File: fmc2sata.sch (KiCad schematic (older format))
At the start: 58 parts, among them J1 ASP-134488-01, J2 1-2199230-6, J3 te-770829-1, Q1 BSS138APW, Q2 BSS138APW, Q3 DMG2305UX-13, Q4 BSS138APW, U1 TPS565208, U2 TPS565208, Y1 AX3DAF1-150.0000

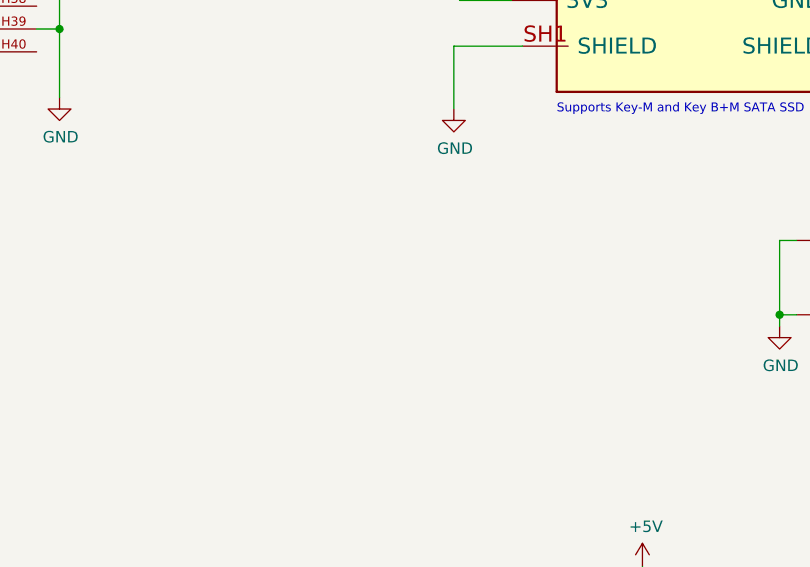
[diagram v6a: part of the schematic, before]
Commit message: Add filtering caps
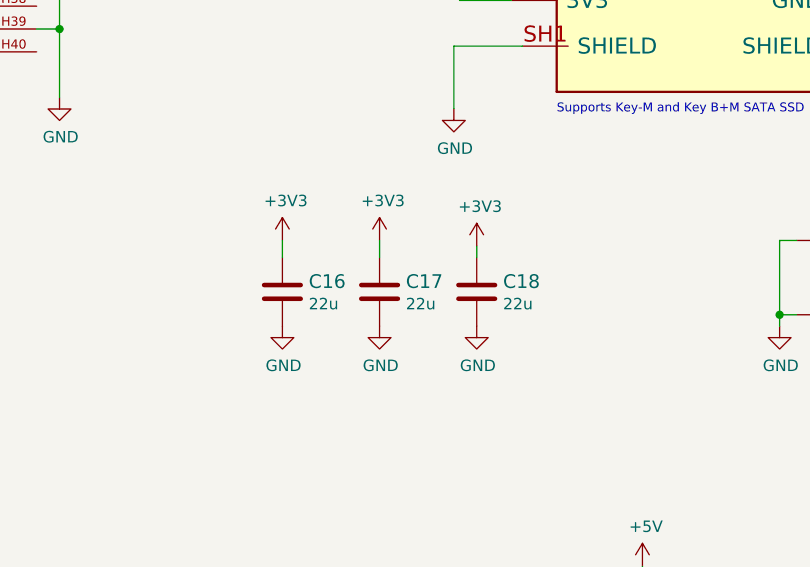
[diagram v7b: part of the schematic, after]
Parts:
- added C16, C17, C18: C_22u_0805_10V, fmc2sata-footprints:0805-cap, symbol fmc2sata:C_22u_0805_10V
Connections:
- net +3V3: now also C16.1, C17.1, C18.1
- net GND: now also C16.2, C17.2, C18.2
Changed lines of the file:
@@
 	0    1    1    0
 $EndComp
+$Comp
+L fmc2sata:C_22u_0805_10V C16
+U 1 1 601D2B63
+P 7150 7725
+F 0 "C16" H 7265 7770 60  0000 L CNN
+F 1 "C_22u_0805_10V" H 7150 7575 60  0001 C CNN
+F 2 "fmc2sata-footprints:0805-cap" H 7350 7925 60  0001 L CNN
+F 3 "" H 7150 7725 50  0001 C CNN
+F 4 "AVX" H 7350 8125 60  0001 L CNN "Manufacturer"
+F 5 "0805ZD226MAT2A" H 7350 8025 60  0001 L CNN "MPN"
+F 6 "22u" H 7265 7672 50  0000 L CNN "Val"
+	1    7150 7725
+	1    0    0    -1
+$EndComp
+$Comp
+L fmc2sata:C_22u_0805_10V C17
+U 1 1 601D4F24
+P 7575 7725
+F 0 "C17" H 7690 7770 60  0000 L CNN
+F 1 "C_22u_0805_10V" H 7575 7575 60  0001 C CNN
+F 2 "fmc2sata-footprints:0805-cap" H 7775 7925 60  0001 L CNN
+F 3 "" H 7575 7725 50  0001 C CNN
+F 4 "AVX" H 7775 8125 60  0001 L CNN "Manufacturer"
+F 5 "0805ZD226MAT2A" H 7775 8025 60  0001 L CNN "MPN"
+F 6 "22u" H 7690 7672 50  0000 L CNN "Val"
+	1    7575 7725
+	1    0    0    -1
+$EndComp
+$Comp
+L fmc2sata:C_22u_0805_10V C18
+U 1 1 601D5219
+P 8000 7725
+F 0 "C18" H 8115 7770 60  0000 L CNN
+F 1 "C_22u_0805_10V" H 8000 7575 60  0001 C CNN
+F 2 "fmc2sata-footprints:0805-cap" H 8200 7925 60  0001 L CNN
+F 3 "" H 8000 7725 50  0001 C CNN
+F 4 "AVX" H 8200 8125 60  0001 L CNN "Manufacturer"
+F 5 "0805ZD226MAT2A" H 8200 8025 60  0001 L CNN "MPN"
+F 6 "22u" H 8115 7672 50  0000 L CNN "Val"
+	1    8000 7725
+	1    0    0    -1
+$EndComp
+$Comp
+L fmc2sata:GND #PWR025
+U 1 1 601D5547
+P 8000 7875
+F 0 "#PWR025" H 8000 7625 50  0001 C CNN
+F 1 "GND" H 8005 7702 50  0000 C CNN
+F 2 "" H 8000 7875 50  0001 C CNN
+F 3 "" H 8000 7875 50  0001 C CNN
+	1    8000 7875
+	1    0    0    -1
+$EndComp
+$Comp
+L fmc2sata:GND #PWR023
+U 1 1 601D58EE
+P 7575 7875
+F 0 "#PWR023" H 7575 7625 50  0001 C CNN
+F 1 "GND" H 7580 7702 50  0000 C CNN
+F 2 "" H 7575 7875 50  0001 C CNN
+F 3 "" H 7575 7875 50  0001 C CNN
+	1    7575 7875
+	1    0    0    -1
+$EndComp
+$Comp
+L fmc2sata:GND #PWR021
+U 1 1 601D5B6B
+P 7150 7875
+F 0 "#PWR021" H 7150 7625 50  0001 C CNN
+F 1 "GND" H 7155 7702 50  0000 C CNN
+F 2 "" H 7150 7875 50  0001 C CNN
+F 3 "" H 7150 7875 50  0001 C CNN
+	1    7150 7875
+	1    0    0    -1
+$EndComp
+$Comp
+L fmc2sata:+3V3 #PWR020
+U 1 1 60202F2A
+P 7150 7500
+F 0 "#PWR020" H 7150 7350 50  0001 C CNN
+F 1 "+3V3" H 7165 7673 50  0000 C CNN
+F 2 "" H 7150 7500 50  0001 C CNN
+F 3 "" H 7150 7500 50  0001 C CNN
+	1    7150 7500
+	1    0    0    -1
+$EndComp
+$Comp
+L fmc2sata:+3V3 #PWR022
+U 1 1 60203855
+P 7575 7500
+F 0 "#PWR022" H 7575 7350 50  0001 C CNN
+F 1 "+3V3" H 7590 7673 50  0000 C CNN
+F 2 "" H 7575 7500 50  0001 C CNN
+F 3 "" H 7575 7500 50  0001 C CNN
+	1    7575 7500
+	1    0    0    -1
+$EndComp
+$Comp
+L fmc2sata:+3V3 #PWR024
+U 1 1 60203CC3
+P 8000 7525
+F 0 "#PWR024" H 8000 7375 50  0001 C CNN
+F 1 "+3V3" H 8015 7698 50  0000 C CNN
+F 2 "" H 8000 7525 50  0001 C CNN
+F 3 "" H 8000 7525 50  0001 C CNN
+	1    8000 7525
+	1    0    0    -1
+$EndComp
+Wire Wire Line
+	8000 7525 8000 7575
+Wire Wire Line
+	7575 7500 7575 7575
+Wire Wire Line
+	7150 7500 7150 7575
 $EndSCHEMATC
